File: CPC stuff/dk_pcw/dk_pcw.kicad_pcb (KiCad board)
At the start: 2 copper layers, 23 parts, among them J1 CONN_25X2, J3 AUDIO-JACK2, J4 DB9, U1 74LS138, U2 74LS74, U3 74LS00, U4 74LS138, U5 AY3-8910

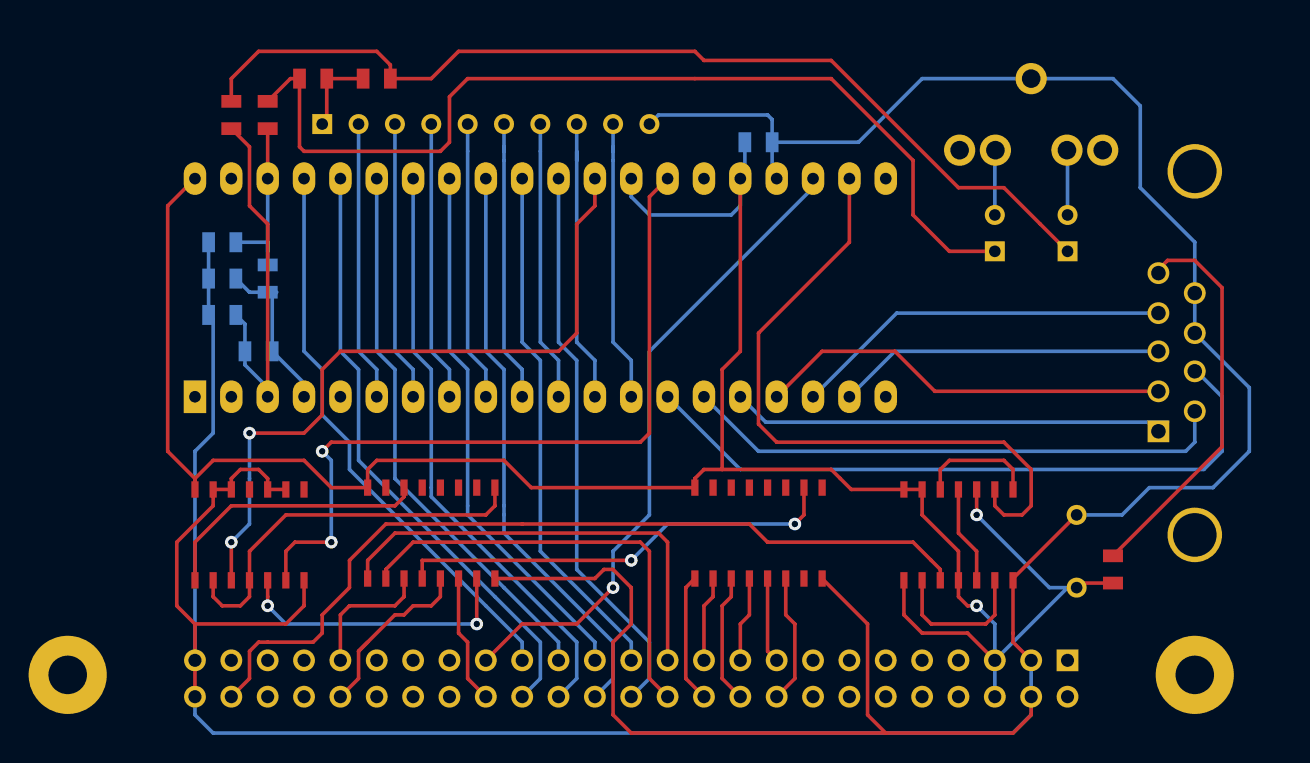
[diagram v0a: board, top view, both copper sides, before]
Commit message: Add clock switch.
When used as an output, IOB0 can be set low to switch the clock to 2MHz.

Also include Gerber files, ready for manufacturing (?)

git-svn-id: svn://pulkomandy.tk/avrstuff@90 c6672c3c-f6b6-47f9-9001-1fd6b12fecbe
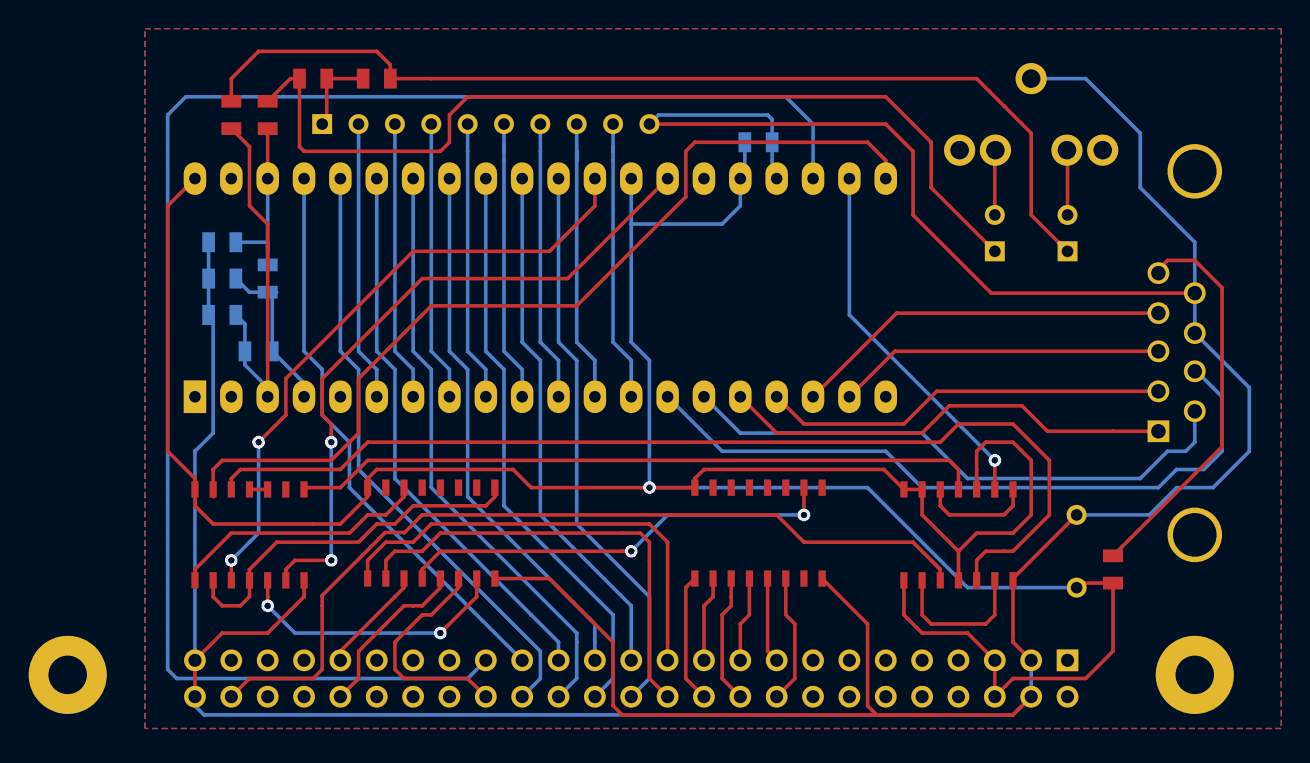
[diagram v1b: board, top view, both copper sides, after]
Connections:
- U2 pad 11: N-0000023 (its old number) -> /CLK24
- U2 pad 5: N-0000023 (its old number) -> /CLK2
- U3 pad 10: GND -> N-0000034
- U3 pad 11: (no net) -> N-0000034
- U3 pad 12: GND -> /CLK2
- U3 pad 13: GND -> /IOA0
- U3 pad 8: (no net) -> /CLK24
- U3 pad 9: GND -> (no net)
- U5 pad 21: (no net) -> /IOA0
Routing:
- net /CLK2: track 0.00 -> 72.1 mm
- net //RESET: track 45.4 -> 112.0 mm, vias 1 -> 0
- net /IOA0: track 0.00 -> 64.3 mm
- net /CLK24: track 0.00 -> 48.3 mm
- net VCC: track 163.5 -> 202.7 mm, vias 2 -> 1
- net /CLK1: track 46.9 -> 25.9 mm, vias 0 -> 1
- net N-0000023 (its old number): track 6.88 -> 0.00 mm
- net /BDIR: track 53.8 -> 47.1 mm
- net //M1: track 9.04 -> 15.7 mm
- net /BC1: track 49.7 -> 44.2 mm
- net GND: track 287.2 -> 284.7 mm
- net N-000004: track 67.5 -> 65.4 mm
- net //RD: track 9.42 -> 7.56 mm
- net N-000005: track 68.7 -> 70.5 mm
- net /IOA6: track 38.3 -> 39.9 mm
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- added copper zone on B.Cu, net GND
- added copper zone on F.Cu, net GND
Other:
- board text added: "AY8930"
- board text added: "DK'Tronics AY interface for PCW"
- board text added: "PulkoTronics 2014 HabiSoft"
